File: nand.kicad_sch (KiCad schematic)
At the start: 5 parts, among them U5 IS21ES08GA-JQLI-TR

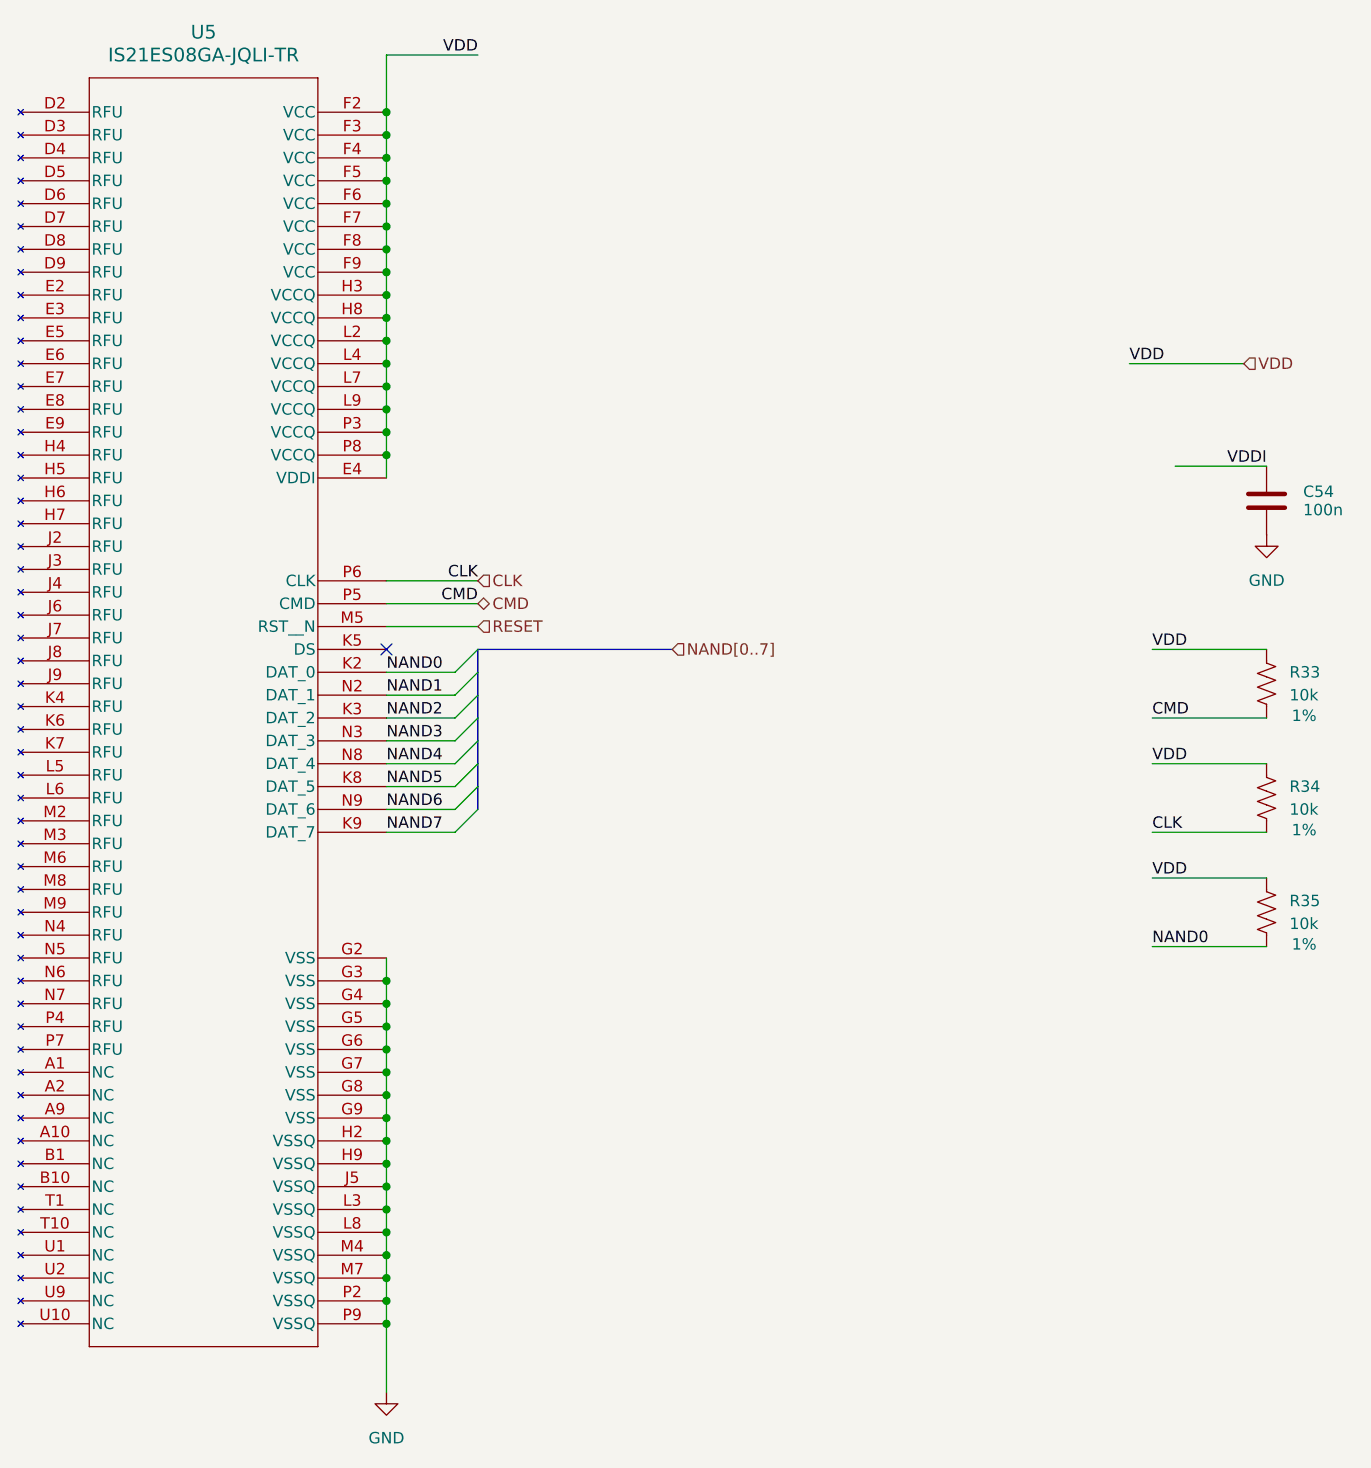
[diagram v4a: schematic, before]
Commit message: Selecting footprints
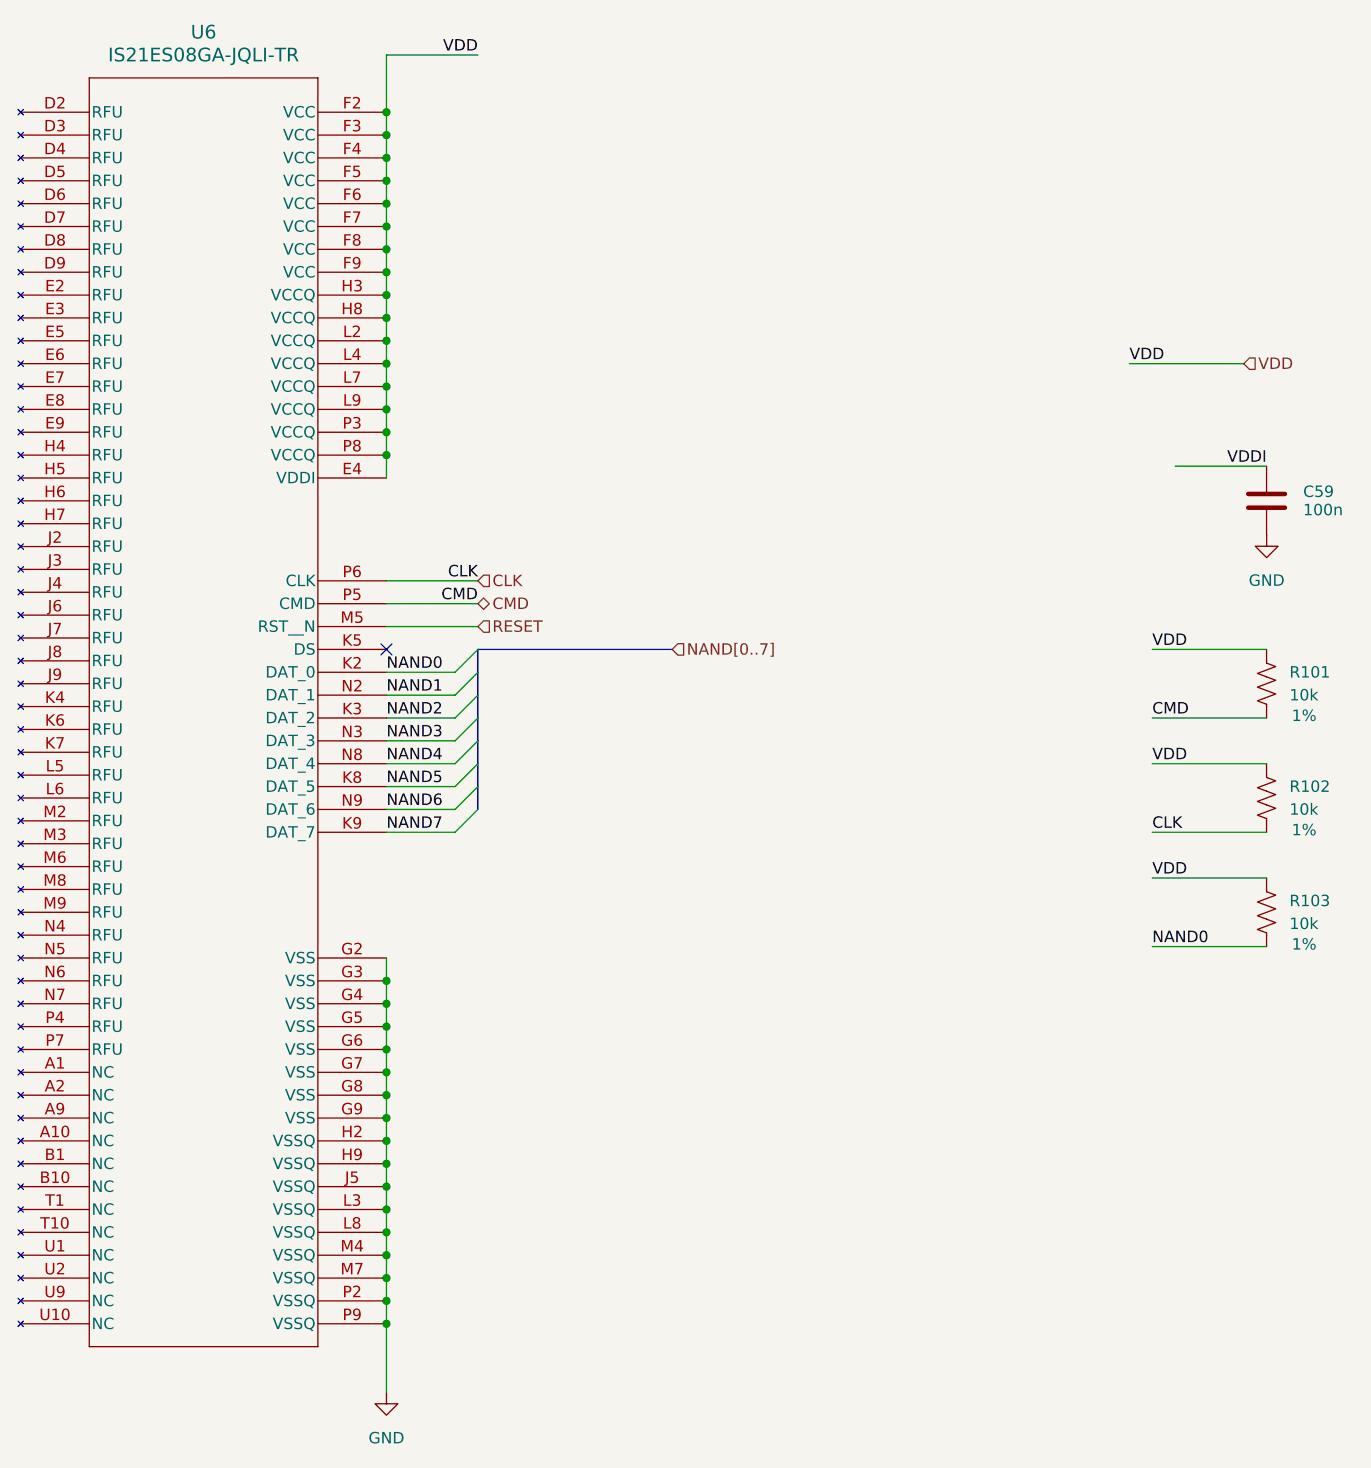
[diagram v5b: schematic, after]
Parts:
- C59: renamed from C54; footprint (none) -> Capacitor_SMD:C_0402_1005Metric
- R101: renamed from R33; footprint (none) -> Capacitor_SMD:C_0402_1005Metric
- R102: renamed from R34; footprint (none) -> Capacitor_SMD:C_0402_1005Metric
- R103: renamed from R35; footprint (none) -> Capacitor_SMD:C_0402_1005Metric
- renumbered U5 to U6
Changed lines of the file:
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@@
 		(on_board yes)
 		(dnp no)
-		(property "Reference" "R34"
+		(property "Reference" "R102"
 			(at 259.08 106.6799 90)
 			(effects
@@
 			)
 		)
-		(property "Footprint" ""
+		(property "Footprint" "Capacitor_SMD:C_0402_1005Metric"
 			(at 261.112 107.95 0)
 			(effects
@@
 			(project "SBC"
 				(path "/21bb932a-ec67-4661-9215-0551f718d1c0/dbc4538f-6782-4334-8773-c54462e4bd8b"
-					(reference "R34")
+					(reference "R102")
 					(unit 1)
 				)
@@
 		(on_board yes)
 		(dnp no)
-		(property "Reference" "R35"
+		(property "Reference" "R103"
 			(at 259.08 119.3799 90)
 			(effects
@@
 			)
 		)
-		(property "Footprint" ""
+		(property "Footprint" "Capacitor_SMD:C_0402_1005Metric"
 			(at 261.112 120.65 0)
 			(effects
@@
 			(project "SBC"
 				(path "/21bb932a-ec67-4661-9215-0551f718d1c0/dbc4538f-6782-4334-8773-c54462e4bd8b"
-					(reference "R35")
+					(reference "R103")
 					(unit 1)
 				)
@@
 		(on_board yes)
 		(dnp no)
-		(property "Reference" "C54"
+		(property "Reference" "C59"
 			(at 260.604 73.914 0)
 			(effects
@@
 			)
 		)
-		(property "Footprint" ""
+		(property "Footprint" "Capacitor_SMD:C_0402_1005Metric"
 			(at 257.5052 86.36 0)
 			(effects
@@
 			(project "SBC"
 				(path "/21bb932a-ec67-4661-9215-0551f718d1c0/dbc4538f-6782-4334-8773-c54462e4bd8b"
-					(reference "C54")
+					(reference "C59")
 					(unit 1)
 				)
@@
 		(dnp no)
 		(fields_autoplaced yes)
-		(property "Reference" "#PWR0116"
+		(property "Reference" "#PWR0196"
 			(at 256.5518 85.0547 0)
 			(effects
@@
 			(project "SBC"
 				(path "/21bb932a-ec67-4661-9215-0551f718d1c0/dbc4538f-6782-4334-8773-c54462e4bd8b"
-					(reference "#PWR0116")
+					(reference "#PWR0196")
 					(unit 1)
 				)
@@
 		(on_board yes)
 		(dnp no)
-		(property "Reference" "R33"
+		(property "Reference" "R101"
 			(at 259.08 93.9799 90)
 			(effects
@@
 			)
 		)
-		(property "Footprint" ""
+		(property "Footprint" "Capacitor_SMD:C_0402_1005Metric"
 			(at 261.112 95.25 0)
 			(effects
@@
 			(project "SBC"
 				(path "/21bb932a-ec67-4661-9215-0551f718d1c0/dbc4538f-6782-4334-8773-c54462e4bd8b"
-					(reference "R33")
+					(reference "R101")
 					(unit 1)
 				)
@@
 		(dnp no)
 		(fields_autoplaced yes)
-		(property "Reference" "U5"
+		(property "Reference" "U6"
 			(at 138.43 22.86 0)
 			(effects
@@
 			(project ""
 				(path "/21bb932a-ec67-4661-9215-0551f718d1c0/dbc4538f-6782-4334-8773-c54462e4bd8b"
-					(reference "U5")
+					(reference "U6")
 					(unit 1)
 				)
@@
 		(dnp no)
 		(fields_autoplaced yes)
-		(property "Reference" "#PWR0117"
+		(property "Reference" "#PWR0197"
 			(at 158.75 180.34 0)
 			(effects
@@
 			(project ""
 				(path "/21bb932a-ec67-4661-9215-0551f718d1c0/dbc4538f-6782-4334-8773-c54462e4bd8b"
-					(reference "#PWR0117")
+					(reference "#PWR0197")
 					(unit 1)
 				)

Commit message: Added all footprints and kicked off pcb design
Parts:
- U6: footprint (none) -> footprints:FBGA100_ISI
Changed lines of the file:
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@@
 			)
 		)
-		(property "Footprint" ""
+		(property "Footprint" "footprints:FBGA100_ISI"
 			(at 138.43 170.434 0)
 			(effects

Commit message: Layout started
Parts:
- renumbered R101 to R115, R102 to R116, R103 to R117
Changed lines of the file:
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@@
 		(on_board yes)
 		(dnp no)
-		(property "Reference" "R102"
+		(property "Reference" "R116"
 			(at 259.08 106.6799 90)
 			(effects
@@
 			(project "SBC"
 				(path "/21bb932a-ec67-4661-9215-0551f718d1c0/dbc4538f-6782-4334-8773-c54462e4bd8b"
-					(reference "R102")
+					(reference "R116")
 					(unit 1)
 				)
@@
 		(on_board yes)
 		(dnp no)
-		(property "Reference" "R103"
+		(property "Reference" "R117"
 			(at 259.08 119.3799 90)
 			(effects
@@
 			(project "SBC"
 				(path "/21bb932a-ec67-4661-9215-0551f718d1c0/dbc4538f-6782-4334-8773-c54462e4bd8b"
-					(reference "R103")
+					(reference "R117")
 					(unit 1)
 				)
@@
 		(dnp no)
 		(fields_autoplaced yes)
-		(property "Reference" "#PWR0196"
+		(property "Reference" "#PWR0218"
 			(at 256.5518 85.0547 0)
 			(effects
@@
 			(project "SBC"
 				(path "/21bb932a-ec67-4661-9215-0551f718d1c0/dbc4538f-6782-4334-8773-c54462e4bd8b"
-					(reference "#PWR0196")
+					(reference "#PWR0218")
 					(unit 1)
 				)
@@
 		(on_board yes)
 		(dnp no)
-		(property "Reference" "R101"
+		(property "Reference" "R115"
 			(at 259.08 93.9799 90)
 			(effects
@@
 			(project "SBC"
 				(path "/21bb932a-ec67-4661-9215-0551f718d1c0/dbc4538f-6782-4334-8773-c54462e4bd8b"
-					(reference "R101")
+					(reference "R115")
 					(unit 1)
 				)
@@
 		(dnp no)
 		(fields_autoplaced yes)
-		(property "Reference" "#PWR0197"
+		(property "Reference" "#PWR0219"
 			(at 158.75 180.34 0)
 			(effects
@@
 			(project ""
 				(path "/21bb932a-ec67-4661-9215-0551f718d1c0/dbc4538f-6782-4334-8773-c54462e4bd8b"
-					(reference "#PWR0197")
+					(reference "#PWR0219")
 					(unit 1)
 				)

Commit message: Component placement
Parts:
- renumbered R115 to R117, R116 to R118, R117 to R119
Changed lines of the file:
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@@
 		(on_board yes)
 		(dnp no)
-		(property "Reference" "R116"
+		(property "Reference" "R118"
 			(at 259.08 106.6799 90)
 			(effects
@@
 			(project "SBC"
 				(path "/21bb932a-ec67-4661-9215-0551f718d1c0/dbc4538f-6782-4334-8773-c54462e4bd8b"
-					(reference "R116")
+					(reference "R118")
 					(unit 1)
 				)
@@
 		(on_board yes)
 		(dnp no)
-		(property "Reference" "R117"
+		(property "Reference" "R119"
 			(at 259.08 119.3799 90)
 			(effects
@@
 			(project "SBC"
 				(path "/21bb932a-ec67-4661-9215-0551f718d1c0/dbc4538f-6782-4334-8773-c54462e4bd8b"
-					(reference "R117")
+					(reference "R119")
 					(unit 1)
 				)
@@
 		(on_board yes)
 		(dnp no)
-		(property "Reference" "R115"
+		(property "Reference" "R117"
 			(at 259.08 93.9799 90)
 			(effects
@@
 			(project "SBC"
 				(path "/21bb932a-ec67-4661-9215-0551f718d1c0/dbc4538f-6782-4334-8773-c54462e4bd8b"
-					(reference "R115")
-					(unit 1)
-				)
+					(reference "R117")
+					(unit 1)
+				)
